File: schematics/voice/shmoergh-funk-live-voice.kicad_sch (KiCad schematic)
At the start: 30 parts, among them Q1 2N3906, U2 TL074, U4 TL074

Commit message: Updated PWM values
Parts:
- R9: value 470k -> about 150k-200k
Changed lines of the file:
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@@
       (effects (font (size 1.27 1.27)))
     )
-    (property "Value" "470k" (at 167.64 134.2136 90)
+    (property "Value" "about 150k-200k" (at 167.64 134.2136 90)
       (effects (font (size 1.27 1.27)))
     )

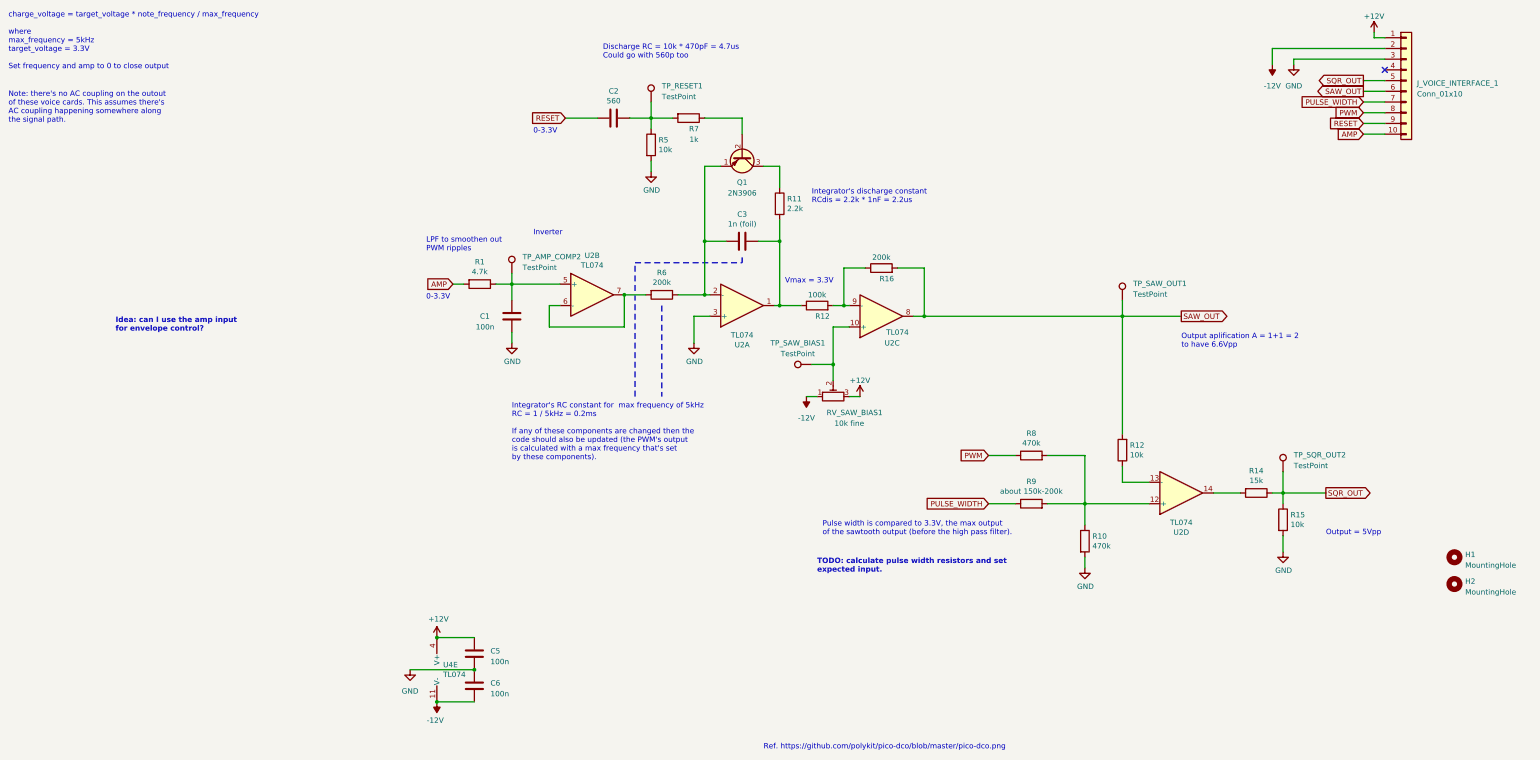
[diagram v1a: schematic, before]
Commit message: Added digital ADSR (untested)
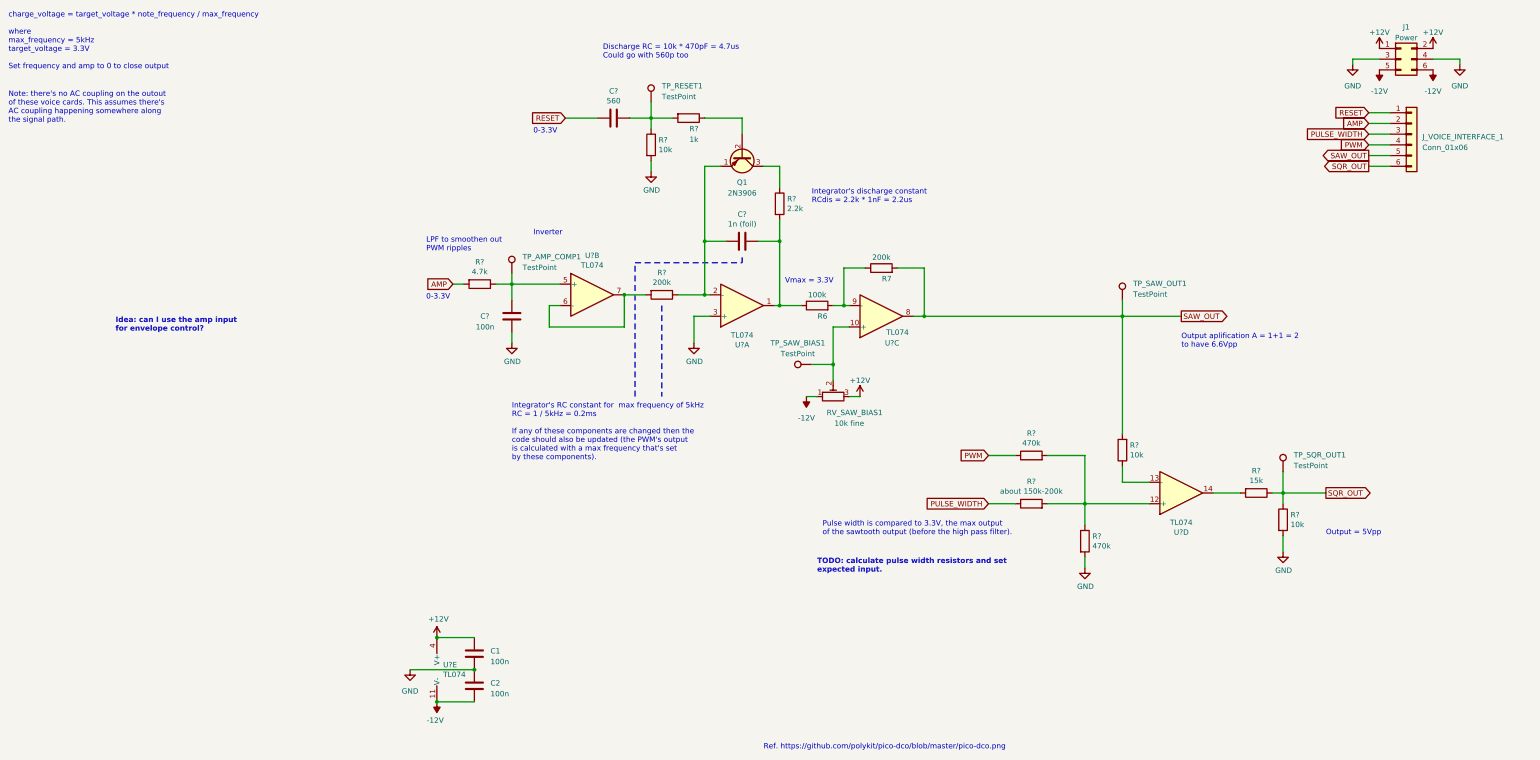
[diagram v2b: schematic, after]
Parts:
- removed H1, H2: MountingHole, MountingHole:MountingHole_3mm_Pad, symbol Mechanical:MountingHole
- removed J_VOICE_INTERFACE_1: Conn_01x10, Connector_PinHeader_2.54mm:PinHeader_1x10_P2.54mm_Vertical, symbol Connector_Generic:Conn_01x10
- added J1: Power, Connector_PinHeader_2.54mm:PinHeader_2x03_P2.54mm_Vertical, symbol Connector_Generic:Conn_02x03_Odd_Even
- added J_VOICE_INTERFACE_1: Conn_01x06, Connector_PinHeader_2.54mm:PinHeader_1x06_P2.54mm_Vertical, symbol Connector_Generic:Conn_01x06
- Q1: footprint Package_TO_SOT_THT_AKL:TO-92_Inline_Wide_EBC -> PCM_Package_TO_SOT_THT_AKL:TO-92L_Inline_Wide
- RV_SAW_BIAS1: footprint (none) -> PCM_Potentiometer_THT_AKL:Potentiometer_ACP_CA6-H2,5_Horizontal
- TP_AMP_COMP1: renamed from TP_AMP_COMP2; footprint (none) -> Connector_Pin:Pin_D0.7mm_L6.5mm_W1.8mm_FlatFork
- TP_RESET1, TP_SAW_BIAS1, TP_SAW_OUT1: footprint (none) -> Connector_Pin:Pin_D0.7mm_L6.5mm_W1.8mm_FlatFork
- TP_SQR_OUT1: renamed from TP_SQR_OUT2; footprint (none) -> Connector_Pin:Pin_D0.7mm_L6.5mm_W1.8mm_FlatFork
- renumbered C5 to C1, C6 to C2, C2 to C?, C3 to C?, C1 to C?, R12 to R6, R16 to R7, R8 to R?, R9 to R?, R7 to R?, R14 to R?, R12 to R?, R15 to R?, R10 to R?, R1 to R?, R5 to R?, R6 to R?, R11 to R?, U2 to U?, U4 to U?
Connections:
- net +12V: now also J1.1 (Pin_1), J1.2 (Pin_2)
- net -12V: now also J1.5 (Pin_5), J1.6 (Pin_6)
- net AMP: now also J_VOICE_INTERFACE_1.2 (Pin_2)
- net GND: now also J1.3 (Pin_3), J1.4 (Pin_4)
- net PULSE_WIDTH: now also J_VOICE_INTERFACE_1.3 (Pin_3)
- net PWM: now also J_VOICE_INTERFACE_1.4 (Pin_4)
- net RESET: now also J_VOICE_INTERFACE_1.1 (Pin_1)
- net SAW_OUT: now also J_VOICE_INTERFACE_1.5 (Pin_5)
- net SQR_OUT: now also J_VOICE_INTERFACE_1.6 (Pin_6)
- no-connect marks 1 -> 0

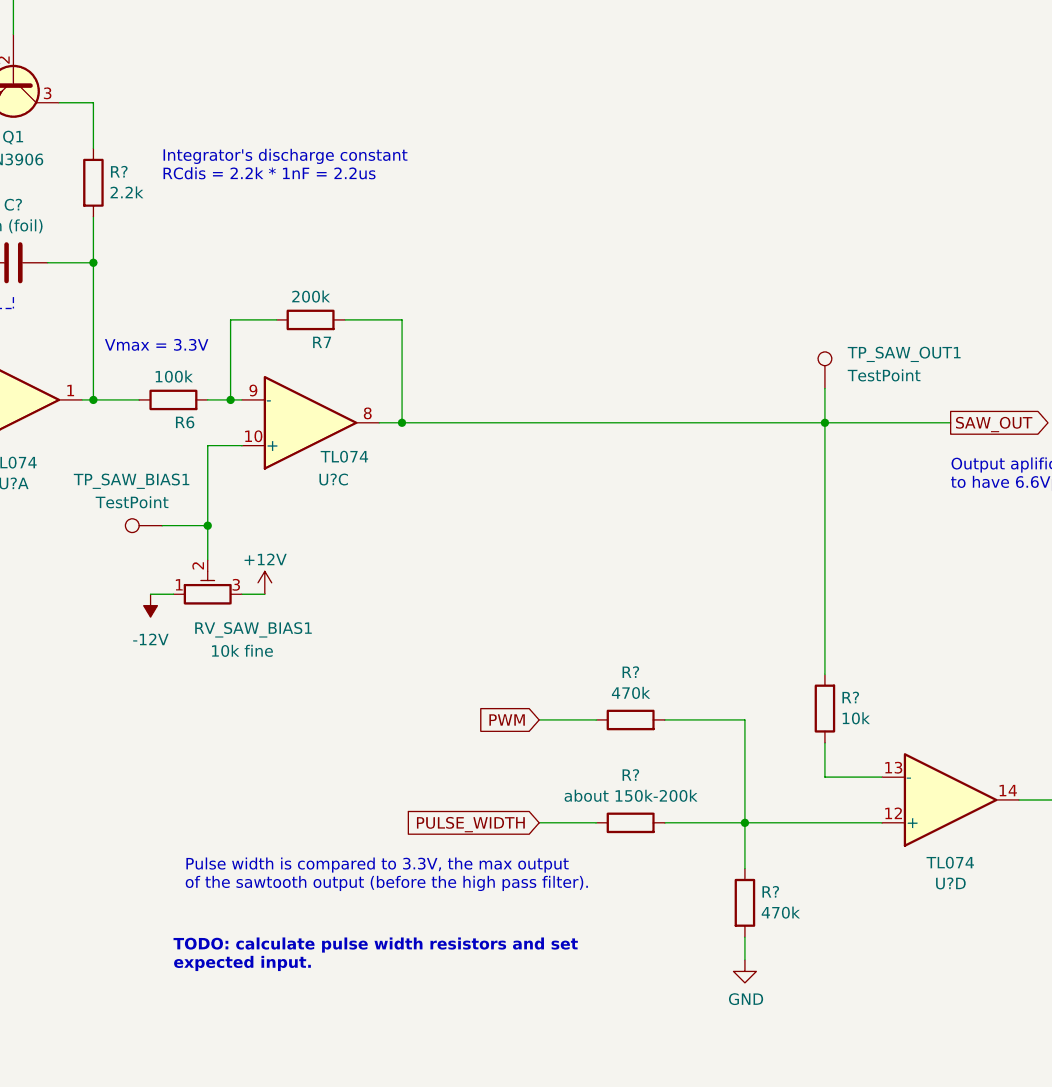
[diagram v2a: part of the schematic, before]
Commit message: Refined voice values
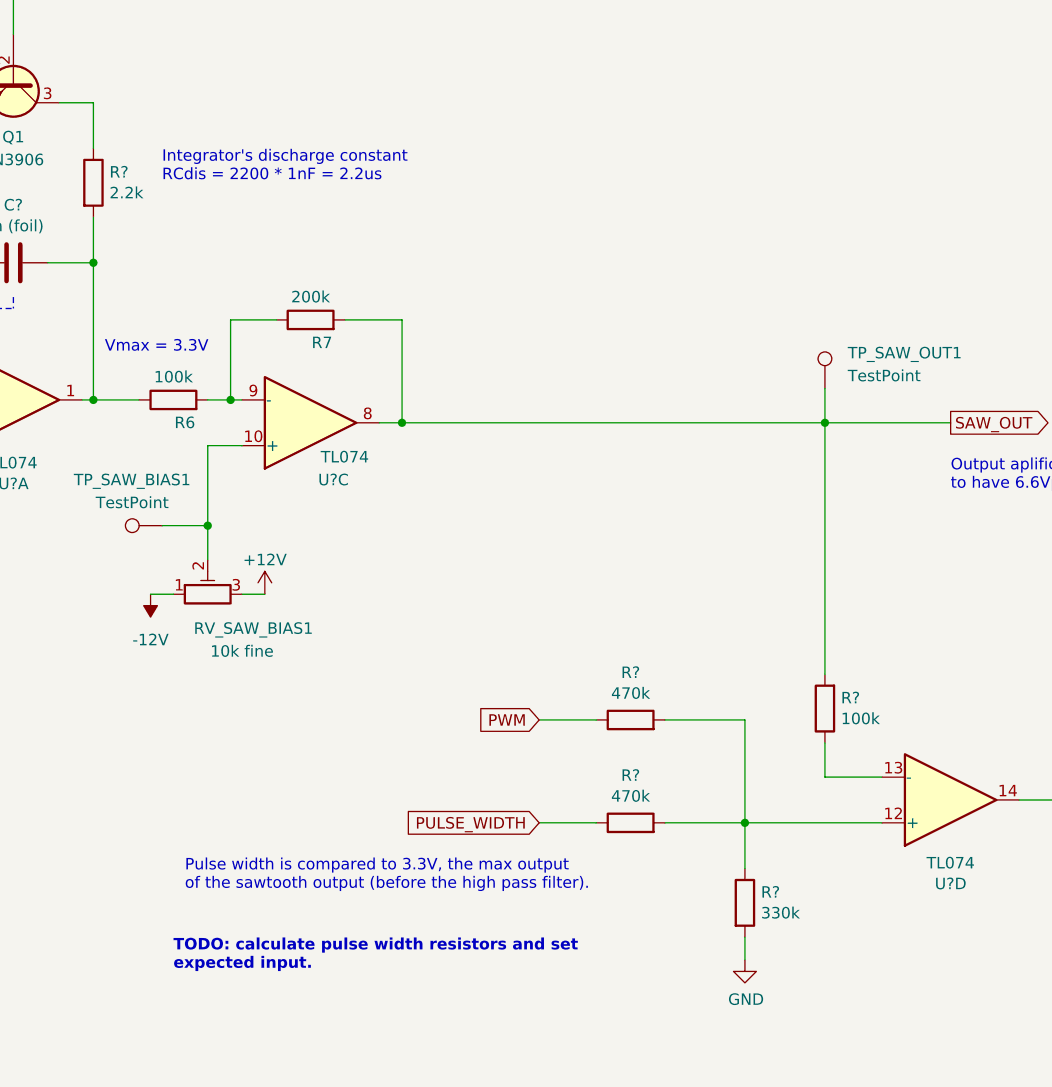
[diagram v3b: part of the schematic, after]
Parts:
- R?: value about 150k-200k -> 470k
- R?: value 10k -> 100k
- R?: value 470k -> 330k
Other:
- note added: "Integrator's discharge constant RCdis = 2200 * 1nF = 2.2us"
- note removed: "Integrator's discharge constant RCdis = 2.2k * 1nF = 2.2us"
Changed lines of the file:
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@@
     (effects (font (size 1.27 1.27)) (justify left bottom))
   )
-  (text "Integrator's discharge constant\nRCdis = 2.2k * 1nF = 2.2us"
+  (text "Integrator's discharge constant\nRCdis = 2200 * 1nF = 2.2us"
     (at 115.57 66.04 0)
     (effects (font (size 1.27 1.27)) (justify left bottom))
@@
       (effects (font (size 1.27 1.27)))
     )
-    (property "Value" "about 150k-200k" (at 167.64 134.2136 90)
+    (property "Value" "470k" (at 167.64 134.2136 90)
       (effects (font (size 1.27 1.27)))
     )
@@
       (effects (font (size 1.27 1.27)) (justify right))
     )
-    (property "Value" "10k" (at 191.008 125.603 0)
+    (property "Value" "100k" (at 191.008 125.603 0)
       (effects (font (size 1.27 1.27)) (justify right))
     )
@@
       (effects (font (size 1.27 1.27)) (justify left))
     )
-    (property "Value" "470k" (at 182.118 147.193 0)
+    (property "Value" "330k" (at 182.118 147.193 0)
       (effects (font (size 1.27 1.27)) (justify left))
     )
